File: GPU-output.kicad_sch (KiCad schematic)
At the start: 19 parts, among them J1 Conn_1-2212115-4, Q1 BSS138PW, Q2 SI7613DN-T1-GE3, Q3 SI7613DN-T1-GE3, U4 TMCS1100A2-Q1

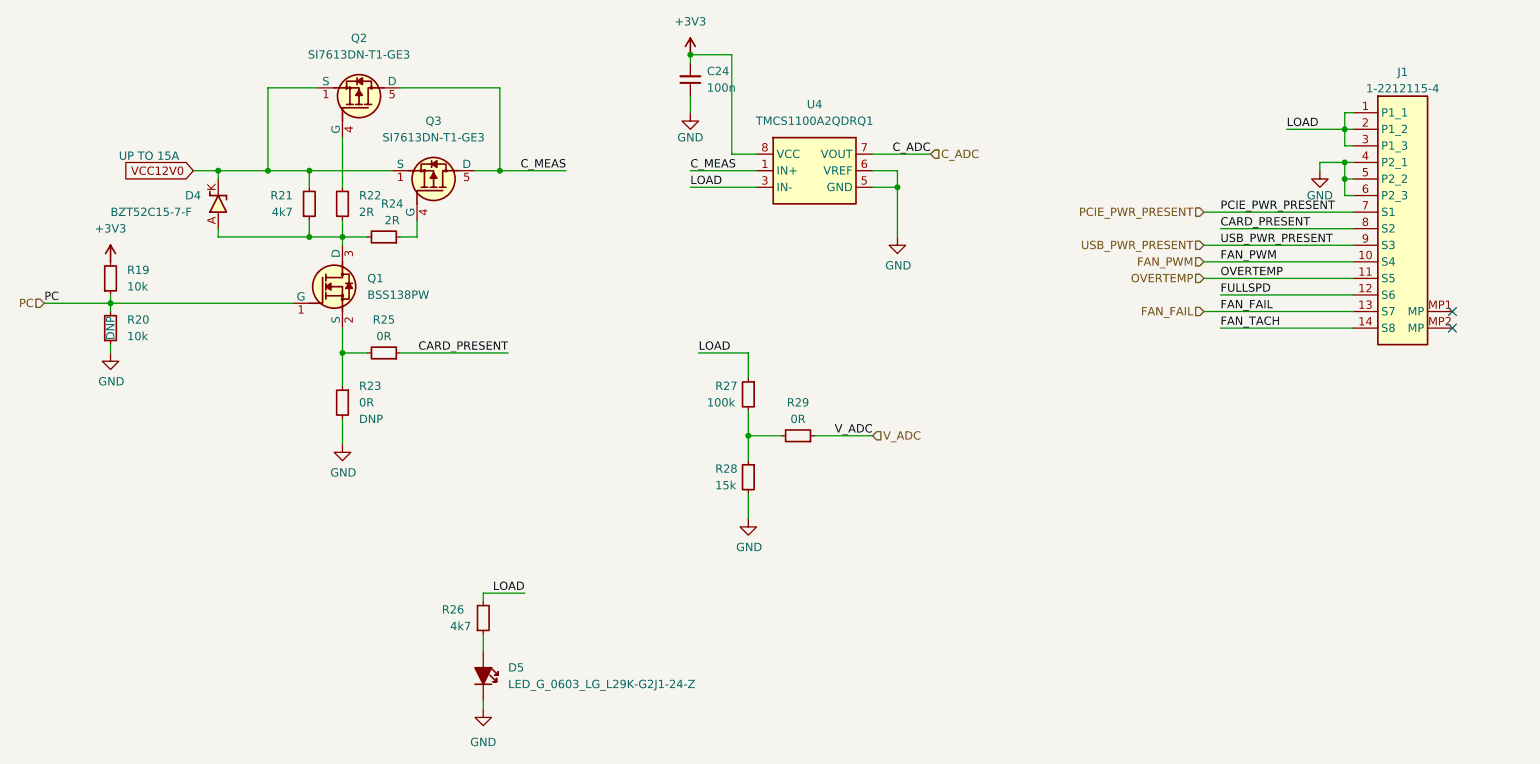
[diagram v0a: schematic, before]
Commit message: Move testpoints to hierarchical sheets
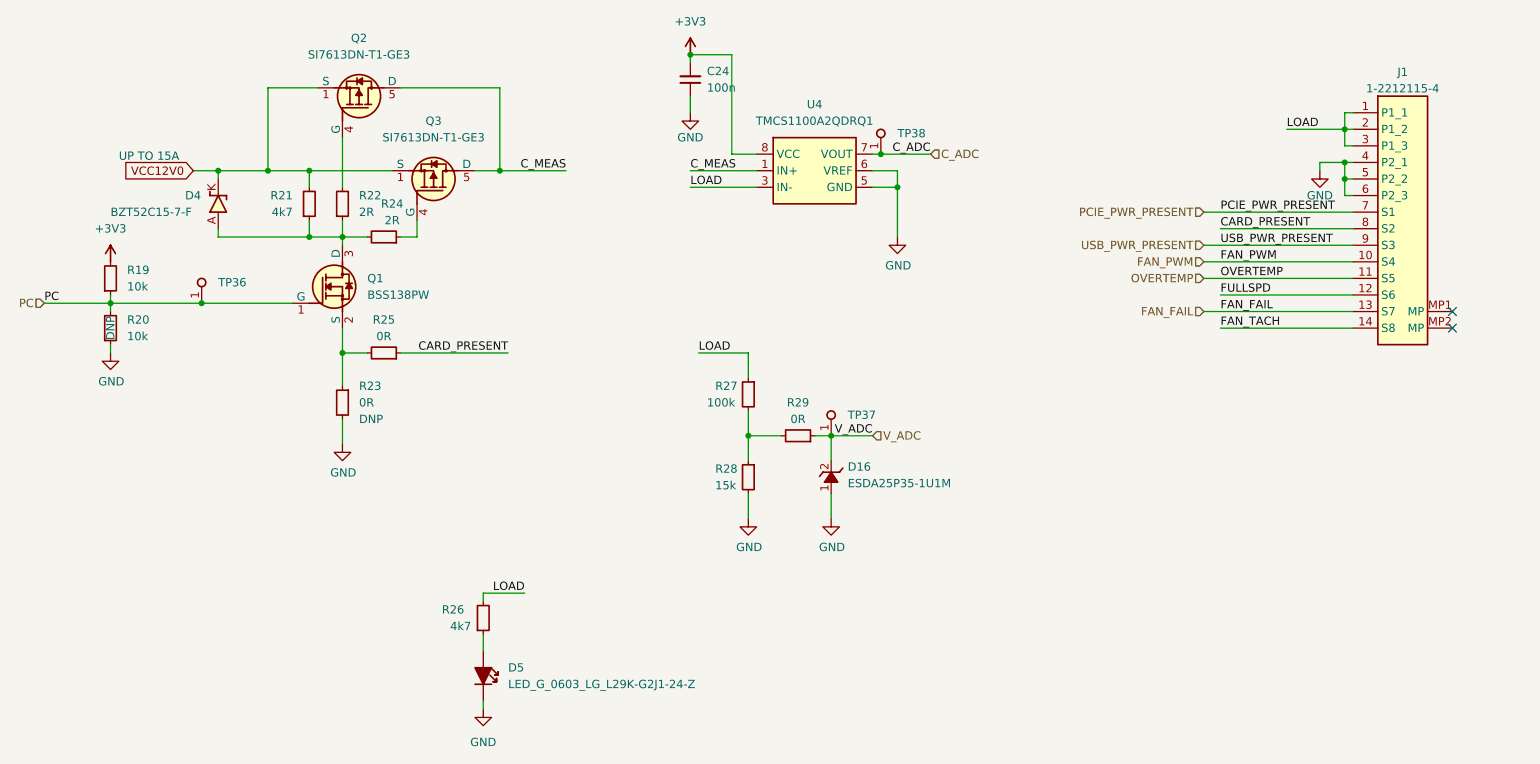
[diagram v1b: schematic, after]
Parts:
- added D16: ESDA25P35-1U1M, antmicro-footprints:ESDA25P35-1U1M, symbol antmicroTVSDiodes:ESDA25P35-1U1M
- added TP36, TP37, TP38: TP_1mm_SMD, antmicro-footprints:TP_SMD_1mm, symbol antmicroTestPoints:TP_1mm_SMD
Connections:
- net C_ADC: now also TP38.1
- net GND: now also D16.1 (K)
- net PC: now also TP36.1
- net V_ADC: now also D16.2 (A), TP37.1
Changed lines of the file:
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@@
   (junction (at 204.47 95.25) (diameter 0) (color 0 0 0 0)
   )
+  (junction (at 233.68 110.49) (diameter 0) (color 0 0 0 0)
+  )
   (junction (at 304.8 106.68) (diameter 0) (color 0 0 0 0)
   )
   (junction (at 151.13 140.97) (diameter 0) (color 0 0 0 0)
   )
+  (junction (at 226.06 153.67) (diameter 0) (color 0 0 0 0)
+  )
+  (junction (at 129.54 133.35) (diameter 0) (color 0 0 0 0)
+  )
   (junction (at 139.7 113.03) (diameter 0) (color 0 0 0 0)
   )
@@
     (stroke (width 0) (type default) (color 0 0 0 0))
   )
-  (wire (pts (xy 115.57 133.35) (xy 143.51 133.35))
+  (wire (pts (xy 115.57 133.35) (xy 129.54 133.35))
     (stroke (width 0) (type default) (color 0 0 0 0))
   )
@@
     (stroke (width 0) (type default) (color 0 0 0 0))
   )
+  (wire (pts (xy 226.06 153.67) (xy 232.41 153.67))
+    (stroke (width 0) (type default) (color 0 0 0 0))
+  )
   (wire (pts (xy 236.22 113.03) (xy 236.22 115.57))
     (stroke (width 0) (type default) (color 0 0 0 0))
@@
     (stroke (width 0) (type default) (color 0 0 0 0))
   )
+  (wire (pts (xy 129.54 133.35) (xy 143.51 133.35))
+    (stroke (width 0) (type default) (color 0 0 0 0))
+  )
   (wire (pts (xy 210.82 110.49) (xy 214.63 110.49))
     (stroke (width 0) (type default) (color 0 0 0 0))
@@
     (stroke (width 0) (type default) (color 0 0 0 0))
   )
-  (wire (pts (xy 223.52 153.67) (xy 232.41 153.67))
+  (wire (pts (xy 223.52 153.67) (xy 226.06 153.67))
+    (stroke (width 0) (type default) (color 0 0 0 0))
+  )
+  (wire (pts (xy 226.06 162.56) (xy 226.06 166.37))
     (stroke (width 0) (type default) (color 0 0 0 0))
   )
@@
     (stroke (width 0) (type default) (color 0 0 0 0))
   )
-  (wire (pts (xy 241.3 110.49) (xy 232.41 110.49))
+  (wire (pts (xy 241.3 110.49) (xy 233.68 110.49))
     (stroke (width 0) (type default) (color 0 0 0 0))
   )
@@
     (stroke (width 0) (type default) (color 0 0 0 0))
   )
+  (wire (pts (xy 233.68 110.49) (xy 232.41 110.49))
+    (stroke (width 0) (type default) (color 0 0 0 0))
+  )
+  (wire (pts (xy 226.06 153.67) (xy 226.06 157.48))
+    (stroke (width 0) (type default) (color 0 0 0 0))
+  )
   (wire (pts (xy 151.13 140.97) (xy 151.13 146.05))
     (stroke (width 0) (type default) (color 0 0 0 0))
@@
     (pin "1")
   )
+  (symbol (lib_id "antmicroTestPoints:TP_1mm_SMD") (at 233.68 110.49 90) (unit 1)
+    (in_bom yes) (on_board yes) (fields_autoplaced)
+    (property "Reference" "TP38" (id 0) (at 236.22 107.3149 90)
+      (effects (font (size 1.27 1.27) (thickness 0.15)) (justify right))
+    )
+    (property "Value" "TP_1mm_SMD" (id 1) (at 241.3 95.25 0)
+      (effects (font (size 1.27 1.27) (thickness 0.15)) (justify left bottom) hide)
+    )
+    (property "Footprint" "antmicro-footprints:TP_SMD_1mm" (id 2) (at 243.84 95.25 0)
+      (effects (font (size 1.27 1.27) (thickness 0.15)) (justify left bottom) hide)
+    )
+    (property "Datasheet" "" (id 3) (at 246.38 92.71 0)
+      (effects (font (size 1.27 1.27) (thickness 0.15)) (justify left bottom) hide)
+    )
+    (property "MPN" "" (id 4) (at 233.68 110.49 0)
+      (effects (font (size 1.27 1.27)) hide)
+    )
+    (property "Manufacturer" "" (id 5) (at 233.68 110.49 0)
+      (effects (font (size 1.27 1.27)) hide)
+    )
+    (property "Author" "Antmicro" (id 6) (at 248.92 95.25 0)
+      (effects (font (size 1.27 1.27) (thickness 0.15)) (justify left bottom) hide)
+    )
+    (property "License" "Apache-2.0" (id 7) (at 251.46 95.25 0)
+      (effects (font (size 1.27 1.27) (thickness 0.15)) (justify left bottom) hide)
+    )
+    (pin "1")
+  )
   (symbol (lib_name "SI7613DN-T1-GE3_1") (lib_id "antmicroTransistorsFETsMOSFETsSingle:SI7613DN-T1-GE3") (at 151.13 107.95 270) (mirror x) (unit 1)
     (in_bom yes) (on_board yes) (fields_autoplaced)
@@
     (pin "1")
   )
+  (symbol (lib_id "antmicroTVSDiodes:ESDA25P35-1U1M") (at 226.06 162.56 90) (unit 1)
+    (in_bom yes) (on_board yes) (fields_autoplaced)
+    (property "Reference" "D16" (id 0) (at 228.6 158.4324 90)
+      (effects (font (size 1.27 1.27) (thickness 0.15)) (justify right))
+    )
+    (property "Value" "ESDA25P35-1U1M" (id 1) (at 228.6 160.9724 90)
+      (effects (font (size 1.27 1.27) (thickness 0.15)) (justify right))
+    )
+    (property "Footprint" "antmicro-footprints:ESDA25P35-1U1M" (id 2) (at 236.22 138.43 0)
+      (effects (font (size 1.27 1.27) (thickness 0.15)) (justify left bottom) hide)
+    )
+    (property "Datasheet" "https://www.st.com/resource/en/datasheet/esda25p35-1u1m.pdf" (id 3) (at 238.76 138.43 0)
+      (effects (font (size 1.27 1.27) (thickness 0.15)) (justify left bottom) hide)
+    )
+    (property "MPN" "ESDA25P35-1U1M" (id 4) (at 241.3 138.43 0)
+      (effects (font (size 1.27 1.27) (thickness 0.15)) (justify left bottom) hide)
+    )
+    (property "Manufacturer" "STMicroelectronics" (id 5) (at 243.84 138.43 0)
+      (effects (font (size 1.27 1.27) (thickness 0.15)) (justify left bottom) hide)
+    )
+    (property "Author" "Antmicro" (id 6) (at 246.38 138.43 0)
+      (effects (font (size 1.27 1.27) (thickness 0.15)) (justify left bottom) hide)
+    )
+    (property "License" "Apache-2.0" (id 7) (at 248.92 138.43 0)
+      (effects (font (size 1.27 1.27) (thickness 0.15)) (justify left bottom) hide)
+    )
+    (pin "1")
+    (pin "2")
+  )
   (symbol (lib_id "antmicroResistors0402:R_15k_0.1%_0402") (at 213.36 157.48 270) (unit 1)
     (in_bom yes) (on_board yes)
@@
     (pin "2")
   )
+  (symbol (lib_id "antmicroTestPoints:TP_1mm_SMD") (at 226.06 153.67 90) (unit 1)
+    (in_bom yes) (on_board yes) (fields_autoplaced)
+    (property "Reference" "TP37" (id 0) (at 228.6 150.4949 90)
+      (effects (font (size 1.27 1.27) (thickness 0.15)) (justify right))
+    )
+    (property "Value" "TP_1mm_SMD" (id 1) (at 233.68 138.43 0)
+      (effects (font (size 1.27 1.27) (thickness 0.15)) (justify left bottom) hide)
+    )
+    (property "Footprint" "antmicro-footprints:TP_SMD_1mm" (id 2) (at 236.22 138.43 0)
+      (effects (font (size 1.27 1.27) (thickness 0.15)) (justify left bottom) hide)
+    )
+    (property "Datasheet" "" (id 3) (at 238.76 135.89 0)
+      (effects (font (size 1.27 1.27) (thickness 0.15)) (justify left bottom) hide)
+    )
+    (property "MPN" "" (id 4) (at 226.06 153.67 0)
+      (effects (font (size 1.27 1.27)) hide)
+    )
+    (property "Manufacturer" "" (id 5) (at 226.06 153.67 0)
+      (effects (font (size 1.27 1.27)) hide)
+    )
+    (property "Author" "Antmicro" (id 6) (at 241.3 138.43 0)
+      (effects (font (size 1.27 1.27) (thickness 0.15)) (justify left bottom) hide)
+    )
+    (property "License" "Apache-2.0" (id 7) (at 243.84 138.43 0)
+      (effects (font (size 1.27 1.27) (thickness 0.15)) (justify left bottom) hide)
+    )
+    (pin "1")
+  )
   (symbol (lib_id "antmicroLEDIndicationDiscrete:LED_G_0603_LG_L29K-G2J1-24-Z") (at 172.72 186.69 270) (unit 1)
     (in_bom yes) (on_board yes) (fields_autoplaced)
@@
     (pin "1")
   )
+  (symbol (lib_id "antmicropower:GND") (at 226.06 166.37 0) (unit 1)
+    (in_bom yes) (on_board yes)
+    (property "Reference" "#PWR0139" (id 0) (at 226.06 172.72 0)
+      (effects (font (size 1.27 1.27)) hide)
+    )
+    (property "Value" "GND" (id 1) (at 226.187 170.7642 0))
+    (property "Footprint" "" (id 2) (at 226.06 166.37 0)
+      (effects (font (size 1.27 1.27)) hide)
+    )
+    (property "Datasheet" "" (id 3) (at 226.06 166.37 0)
+      (effects (font (size 1.27 1.27)) hide)
+    )
+    (pin "1")
+  )
   (symbol (lib_id "antmicroPowerMeasurement:TMCS1100A2-Q1") (at 214.63 110.49 0) (unit 1)
     (in_bom yes) (on_board yes) (fields_autoplaced)
@@
     (pin "2")
   )
+  (symbol (lib_id "antmicroTestPoints:TP_1mm_SMD") (at 129.54 133.35 90) (unit 1)
+    (in_bom yes) (on_board yes) (fields_autoplaced)
+    (property "Reference" "TP36" (id 0) (at 132.08 130.1749 90)
+      (effects (font (size 1.27 1.27) (thickness 0.15)) (justify right))
+    )
+    (property "Value" "TP_1mm_SMD" (id 1) (at 137.16 118.11 0)
+      (effects (font (size 1.27 1.27) (thickness 0.15)) (justify left bottom) hide)
+    )
+    (property "Footprint" "antmicro-footprints:TP_SMD_1mm" (id 2) (at 139.7 118.11 0)
+      (effects (font (size 1.27 1.27) (thickness 0.15)) (justify left bottom) hide)
+    )
+    (property "Datasheet" "" (id 3) (at 142.24 115.57 0)
+      (effects (font (size 1.27 1.27) (thickness 0.15)) (justify left bottom) hide)
+    )
+    (property "MPN" "" (id 4) (at 129.54 133.35 0)
+      (effects (font (size 1.27 1.27)) hide)
+    )
+    (property "Manufacturer" "" (id 5) (at 129.54 133.35 0)
+      (effects (font (size 1.27 1.27)) hide)
+    )
+    (property "Author" "Antmicro" (id 6) (at 144.78 118.11 0)
+      (effects (font (size 1.27 1.27) (thickness 0.15)) (justify left bottom) hide)
+    )
+    (property "License" "Apache-2.0" (id 7) (at 147.32 118.11 0)
+      (effects (font (size 1.27 1.27) (thickness 0.15)) (justify left bottom) hide)
+    )
+    (pin "1")
+  )
   (symbol (lib_name "R_0R_0402_1") (lib_id "antmicroResistors0402:R_0R_0402") (at 151.13 146.05 270) (unit 1)

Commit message: Draft component placement for all fan control
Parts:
- U4: footprint antmicro-footprints:SOIC-8-1EP_3.9x4.9x1.75mm_P1.27mm -> antmicro-footprints:SOIC-8_3.9x4.9x1.75mm_P1.27mm
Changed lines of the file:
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@@
     (pin "5")
+  )
+  (symbol (lib_name "TMCS1100A2-Q1_1") (lib_id "antmicroPowerMeasurement:TMCS1100A2-Q1") (at 214.63 110.49 0) (unit 1)
+    (in_bom yes) (on_board yes) (fields_autoplaced)
+    (property "Reference" "U4" (id 0) (at 223.52 102.87 0)
+      (effects (font (size 1.27 1.27) (thickness 0.15)))
+    )
+    (property "Value" "TMCS1100A2-Q1" (id 1) (at 247.65 118.11 0)
+      (effects (font (size 1.27 1.27) (thickness 0.15)) (justify left bottom) hide)
+    )
+    (property "Footprint" "antmicro-footprints:SOIC-8_3.9x4.9x1.75mm_P1.27mm" (id 2) (at 247.65 120.65 0)
+      (effects (font (size 1.27 1.27) (thickness 0.15)) (justify left bottom) hide)
+    )
+    (property "Datasheet" "https://www.ti.com/lit/ds/symlink/tmcs1100-q1.pdf?ts=1647195769204&ref_url=https%253A%252F%252Fwww.mouser.de%252F" (id 3) (at 247.65 123.19 0)
+      (effects (font (size 1.27 1.27) (thickness 0.15)) (justify left bottom) hide)
+    )
+    (property "MPN" "TMCS1100A2QDRQ1" (id 4) (at 223.52 105.41 0)
+      (effects (font (size 1.27 1.27) (thickness 0.15)))
+    )
+    (property "Manufacturer" "Texas Instruments" (id 5) (at 247.65 125.73 0)
+      (effects (font (size 1.27 1.27) (thickness 0.15)) (justify left bottom) hide)
+    )
+    (property "Author" "Antmicro" (id 6) (at 247.65 128.27 0)
+      (effects (font (size 1.27 1.27) (thickness 0.15)) (justify left bottom) hide)
+    )
+    (property "License" "Apache-2.0" (id 7) (at 247.65 130.81 0)
+      (effects (font (size 1.27 1.27) (thickness 0.15)) (justify left bottom) hide)
+    )
+    (pin "1")
+    (pin "2")
+    (pin "3")
+    (pin "4")
+    (pin "5")
+    (pin "6")
+    (pin "7")
+    (pin "8")
   )
   (symbol (lib_id "antmicropower:+3V3") (at 204.47 95.25 0) (unit 1)
@@
     (pin "1")
   )
-  (symbol (lib_id "antmicroPowerMeasurement:TMCS1100A2-Q1") (at 214.63 110.49 0) (unit 1)
-    (in_bom yes) (on_board yes) (fields_autoplaced)
-    (property "Reference" "U4" (id 0) (at 223.52 102.87 0)
-      (effects (font (size 1.27 1.27) (thickness 0.15)))
-    )
-    (property "Value" "TMCS1100A2-Q1" (id 1) (at 247.65 118.11 0)
-      (effects (font (size 1.27 1.27) (thickness 0.15)) (justify left bottom) hide)
-    )
-    (property "Footprint" "antmicro-footprints:SOIC-8-1EP_3.9x4.9x1.75mm_P1.27mm" (id 2) (at 247.65 120.65 0)
-      (effects (font (size 1.27 1.27) (thickness 0.15)) (justify left bottom) hide)
-    )
-    (property "Datasheet" "https://www.ti.com/lit/ds/symlink/tmcs1100-q1.pdf?ts=1647195769204&ref_url=https%253A%252F%252Fwww.mouser.de%252F" (id 3) (at 247.65 123.19 0)
-      (effects (font (size 1.27 1.27) (thickness 0.15)) (justify left bottom) hide)
-    )
-    (property "MPN" "TMCS1100A2QDRQ1" (id 4) (at 223.52 105.41 0)
-      (effects (font (size 1.27 1.27) (thickness 0.15)))
-    )
-    (property "Manufacturer" "Texas Instruments" (id 5) (at 247.65 125.73 0)
-      (effects (font (size 1.27 1.27) (thickness 0.15)) (justify left bottom) hide)
-    )
-    (property "Author" "Antmicro" (id 6) (at 247.65 128.27 0)
-      (effects (font (size 1.27 1.27) (thickness 0.15)) (justify left bottom) hide)
-    )
-    (property "License" "Apache-2.0" (id 7) (at 247.65 130.81 0)
-      (effects (font (size 1.27 1.27) (thickness 0.15)) (justify left bottom) hide)
-    )
-    (pin "1")
-    (pin "2")
-    (pin "3")
-    (pin "4")
-    (pin "5")
-    (pin "6")
-    (pin "7")
-    (pin "8")
-  )
   (symbol (lib_id "antmicropower:GND") (at 213.36 166.37 0) (unit 1)
